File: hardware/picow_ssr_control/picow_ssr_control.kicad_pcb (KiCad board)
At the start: 2 copper layers, 65 x 90 mm, 25 parts, among them Q1 IRF4905, U1 RaspberryPi-PicoW, U2 ULN2803A

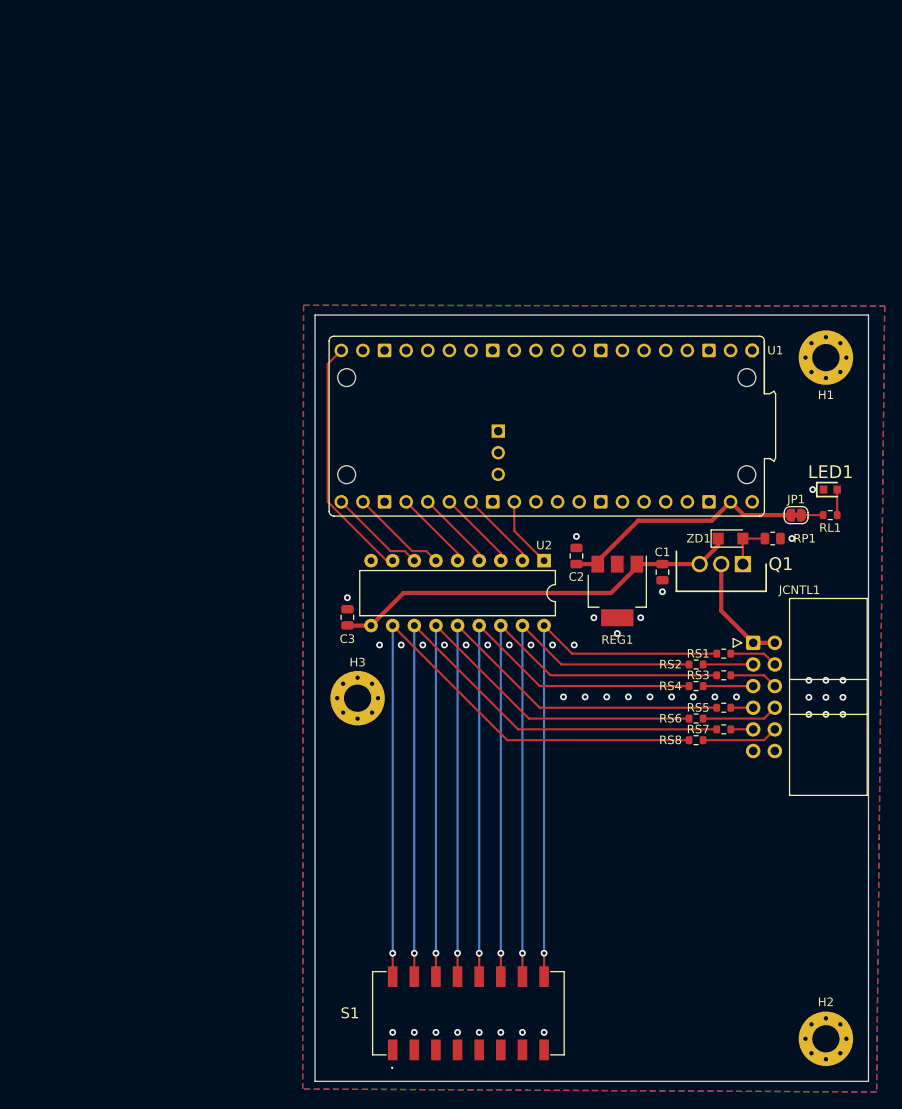
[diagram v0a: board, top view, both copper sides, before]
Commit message: Added Copyright and logos etc.
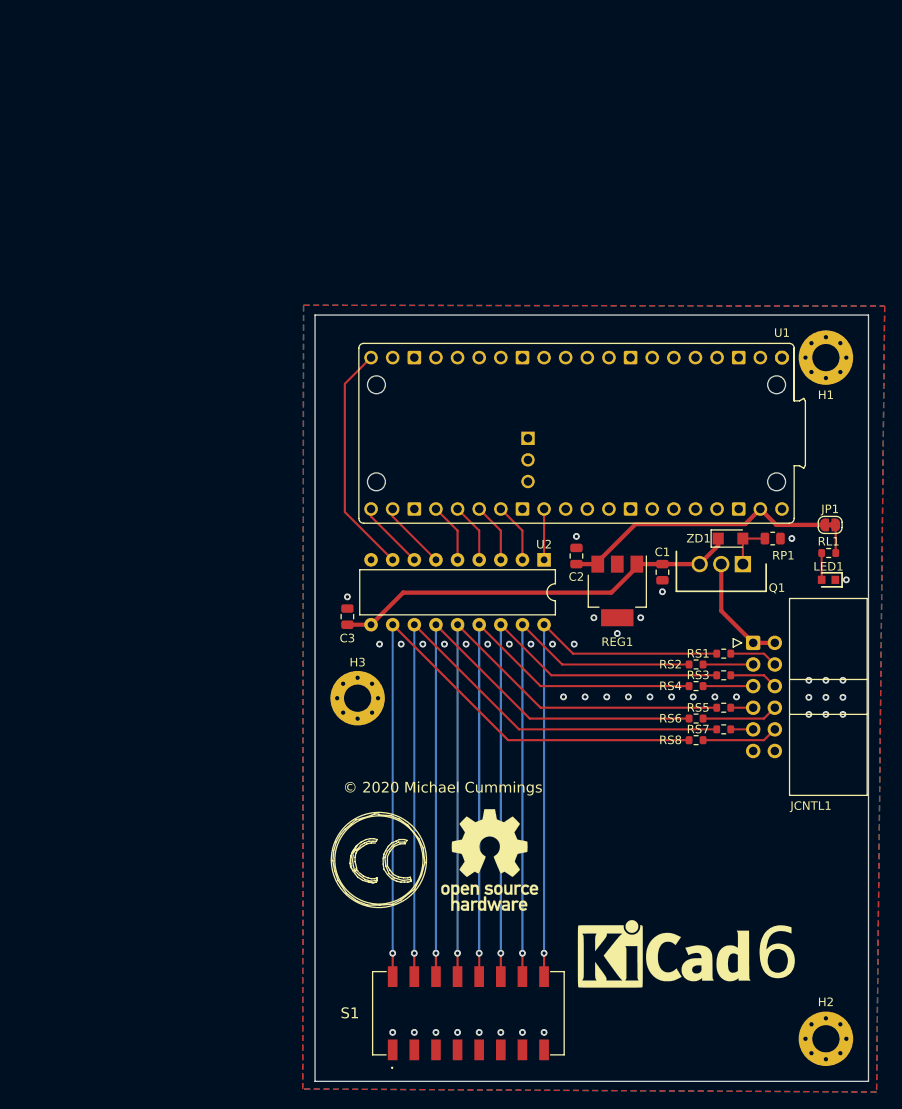
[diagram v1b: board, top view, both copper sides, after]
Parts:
- added #LOGO1: OSHW-Logo_11.4x12mm_SilkScreen, Symbol:OSHW-Logo_11.4x12mm_SilkScreen, F.Cu at (70.5, 114.0)
- added #LOGO2: KiCad-Logo_8mm_SilkScreen, Symbol:KiCad-Logo_8mm_SilkScreen, F.Cu at (91.0, 125.0)
- added #LOGO2: Symbol_CreativeCommons_SilkScreenTop_Type2_Big, Symbol:Symbol_CreativeCommons_SilkScreenTop_Type2_Big, F.Cu at (57.5, 114.0)
- moved LED1 10.6 mm to (110.3, 81.1), turned to 180 degrees
- moved RL1 4.45 mm to (110.3, 78.0), turned to 180 degrees
- moved JP1 4.16 mm to (110.5, 74.7)
- moved U1 3.59 mm to (104.8, 55.0)
- moved U2 0.10 mm to (76.9, 78.8)
- moved C3 0.08 mm to (53.8, 85.4)
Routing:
- net +5V: track 29.0 -> 32.5 mm
- net Net-(U1-Pad22): track 11.4 -> 8.07 mm
- net Net-(U1-Pad21): track 11.4 -> 8.07 mm
- net Net-(U1-Pad29): track 8.36 -> 5.97 mm
- net Net-(U1-Pad26): track 9.41 -> 7.02 mm
- net Net-(U1-Pad24): track 9.41 -> 7.02 mm
- net Net-(U1-Pad25): track 9.41 -> 7.02 mm
- net Net-(U1-Pad27): track 9.41 -> 7.02 mm
- net Net-(U1-Pad20): track 28.9 -> 27.4 mm
- net Net-(JP1-Pad2): track 2.52 -> 3.30 mm
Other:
- board text added: "0.2000 mm / 0.0000 mm"
- board text added: "0.3000 mm"
- board text added: "1.7600 mm"
- board text added: "2"
- board text added: "6"
- board text added: "65.0000 mm x 90.0000 mm"
- board text added: "BOARD CHARACTERISTICS"
- board text added: "Board Thickness:"
- board text added: "Board overall dimensions:"
- board text added: "Castellated pads:"
- board text added: "Copper Finish:"
- board text added: "Copper Layer Count:"
- board text added: "Edge card connectors:"
- board text added: "HAL lead-free"
- board text added: "Impedance Control:"
- board text added: "Min hole diameter:"
- board text added: "Min track/spacing:"
- board text added: "No"
- board text added: "Plated Board Edge:"
- board text added: "© 2020 Michael Cummings"

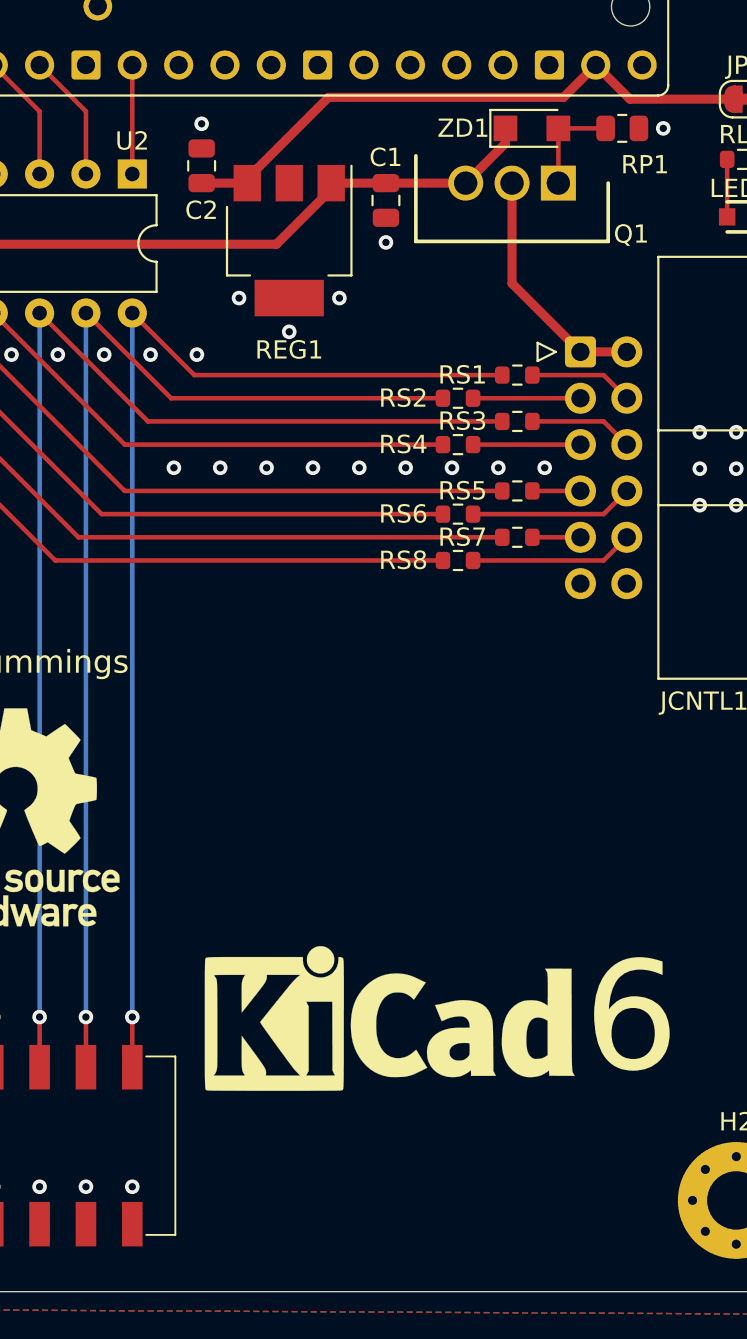
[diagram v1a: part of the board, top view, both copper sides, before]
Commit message: Added Updated symbol, footprint, 3d model for zener diode
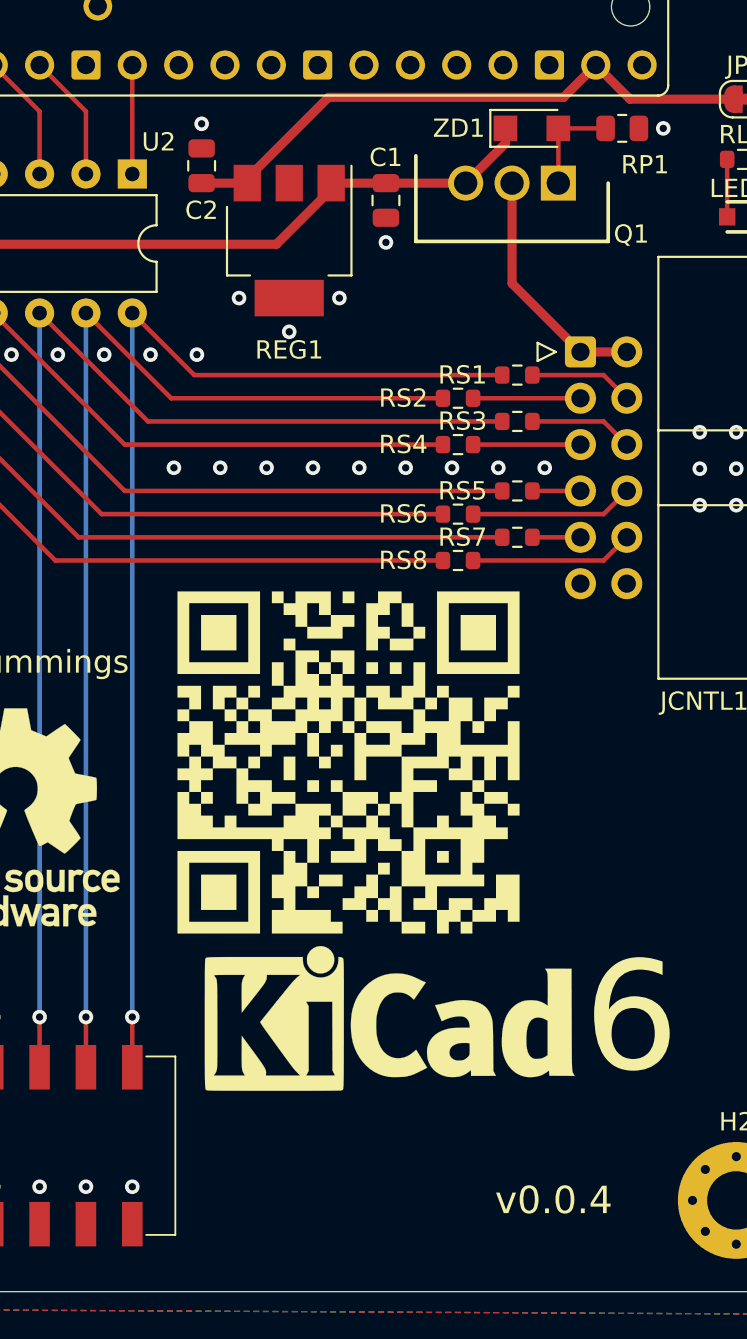
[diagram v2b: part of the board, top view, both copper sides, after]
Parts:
- added QRCode1: LOGO, LOGO, F.Cu at (88.8, 111.0)
- ZD1: footprint Diode_SMD:D_SMF -> Picow_control:BZD27C10P-M3-08
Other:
- board text added: "v0.0.4"

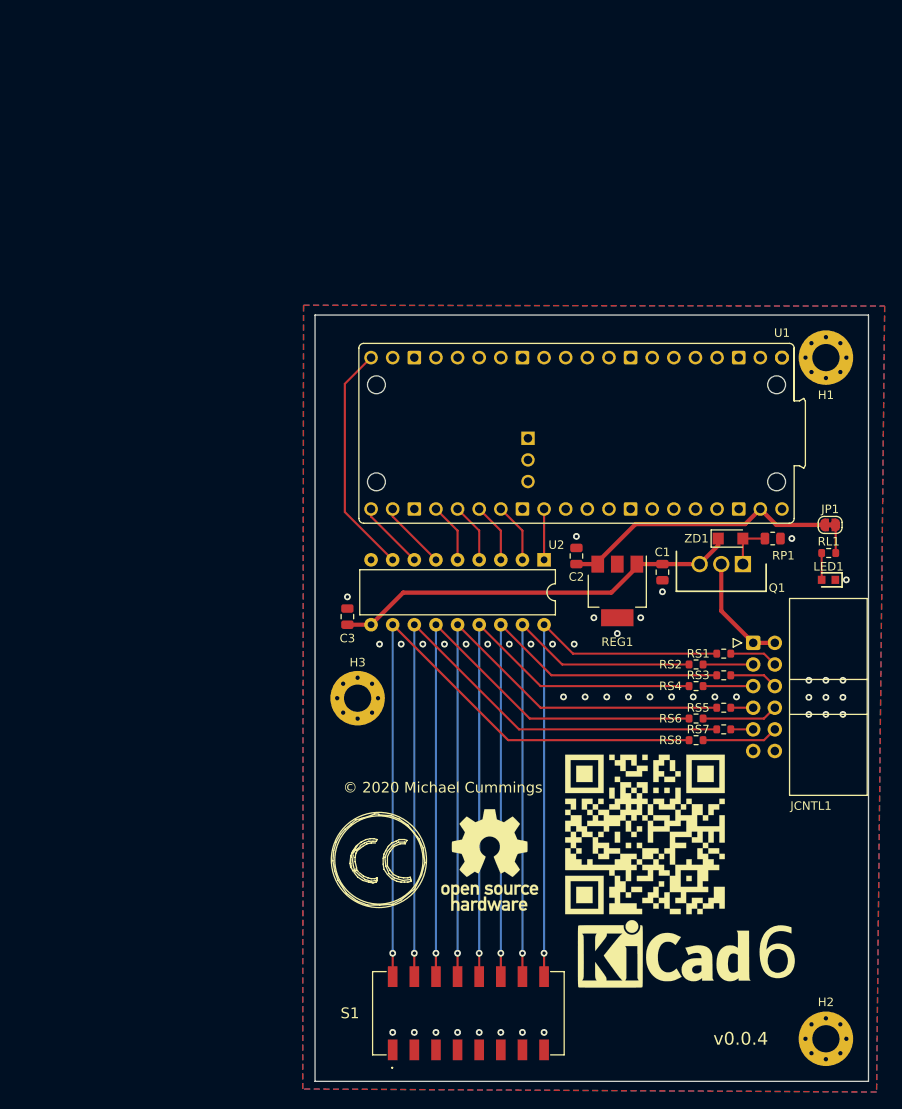
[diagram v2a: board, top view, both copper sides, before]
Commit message: Add new Cern licensing info
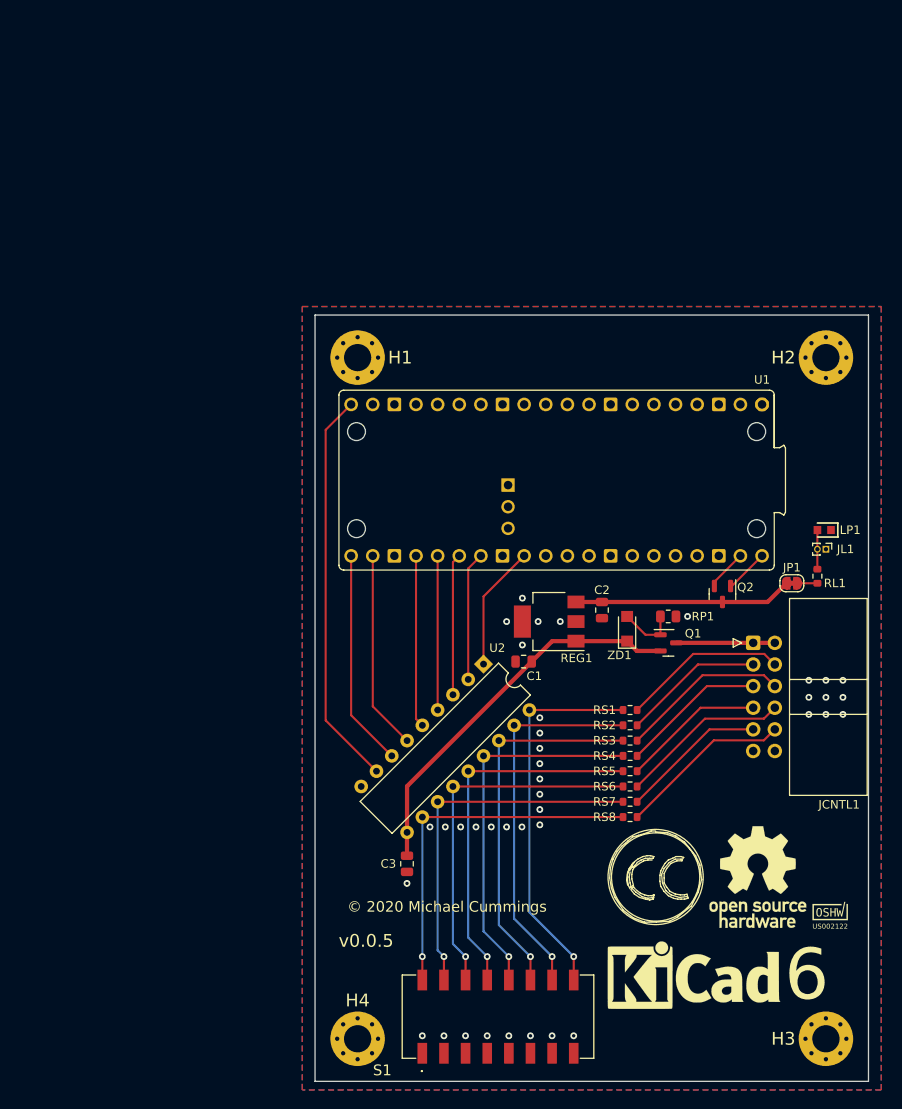
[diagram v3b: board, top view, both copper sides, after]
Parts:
- removed LED1: LTST-C190KGKT, dragon_mobile:LEDC1608X80N
- added H4: MountingHole_Pad, MountingHole:MountingHole_3.2mm_M3_Pad_Via, F.Cu at (55.0, 135.0)
- added JL1: Conn_01x02, Connector_PinHeader_1.00mm:PinHeader_1x02_P1.00mm_Vertical, F.Cu at (110.0, 77.5)
- added LP1: LTST-C190KGKT, dragon_mobile:LEDC1608X80N, F.Cu at (109.8, 75.2)
- added OSHW_Mono_0.1_Scale: US002122, Picow_control:OSHW_Mono_0.1_Scale, F.Cu at (110.5, 120.0)
- added Q2: DMG2301L, Package_TO_SOT_SMD:SOT-23, F.Cu at (97.8, 82.8)
- Q1: value IRF4905 -> DMG2301L; footprint dragon_mobile:TO254P469X1042X1967-3P -> Package_TO_SOT_SMD:SOT-23
- QRCode1: moved to B.Cu
- moved H2 80.0 mm to (110.0, 55.0)
- moved H3 68.0 mm to (110.0, 135.0)
- moved H1 55.0 mm to (55.0, 55.0)
- moved #LOGO2 32.6 mm to (90.0, 116.0)
- moved #LOGO1 31.6 mm to (102.0, 116.0)
- moved C3 29.9 mm to (60.8, 114.5), turned to -90 degrees
- moved C1 19.4 mm to (74.5, 90.7), turned to 180 degrees
- moved ZD1 16.1 mm to (86.7, 86.8), turned to 90 degrees
- moved RP1 15.3 mm to (91.5, 85.4)
- moved U2 14.2 mm to (69.8, 91.0), turned to -45 degrees
- moved RS7 13.9 mm to (87.0, 107.2)
- moved RS3 13.4 mm to (87.0, 100.0)
- moved RS5 13.3 mm to (87.0, 103.6)
- moved RS1 12.8 mm to (87.0, 96.4)
- moved Q1 12.7 mm to (91.5, 88.5), turned to 0 degrees
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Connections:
- Q1 pad 2: +BATT -> +VDC
- Q1 pad 3: +VDC -> +BATT
- U1 pad 39: +5V -> Net-(Q2-Pad2)
- U1 pad 40: unconnected-(U1-Pad40) -> Net-(Q2-Pad1)
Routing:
- net /a8: track 81.8 -> 42.7 mm
- net /a7: track 81.9 -> 43.0 mm
- net /a6: track 75.6 -> 43.3 mm
- net /a5: track 75.8 -> 43.6 mm
- net /a4: track 69.0 -> 43.9 mm
- net /a3: track 69.1 -> 44.2 mm
- net Net-(U1-Pad20): track 27.4 -> 46.8 mm
- net /a2: track 62.8 -> 44.6 mm
- net /a1: track 63.0 -> 44.9 mm
- net Net-(U1-Pad21): track 8.07 -> 25.5 mm
- net Net-(U1-Pad22): track 8.07 -> 23.4 mm
- net Net-(JCNTL1-Pad9): track 2.63 -> 17.2 mm
- net Net-(JCNTL1-Pad6): track 5.70 -> 19.9 mm
- net Net-(JCNTL1-Pad7): track 2.63 -> 16.7 mm
- net Net-(JCNTL1-Pad4): track 5.70 -> 19.4 mm
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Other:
- board text added: "+"
- board text added: "Mounting holes are for M3 screws and should be drill at 2.5mm (#39) and tapped at .5mm threads."
- board text added: "v0.0.5"
- board text removed: "v0.0.4"

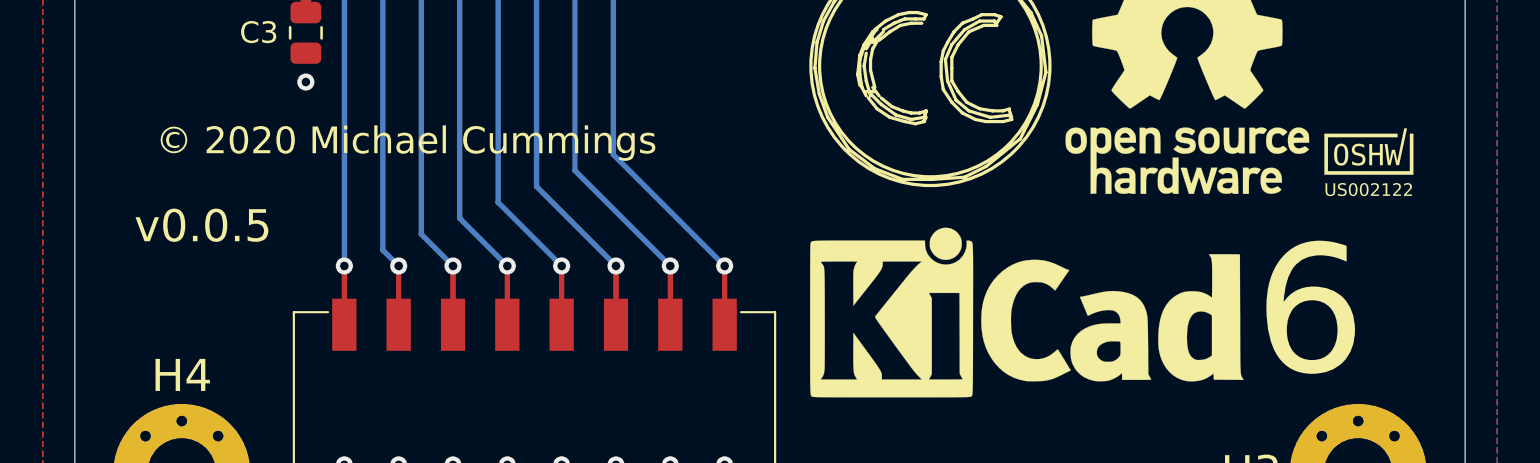
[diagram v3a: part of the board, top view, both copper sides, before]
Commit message: Synced up schema and PCB versions and Licensing silkscreening
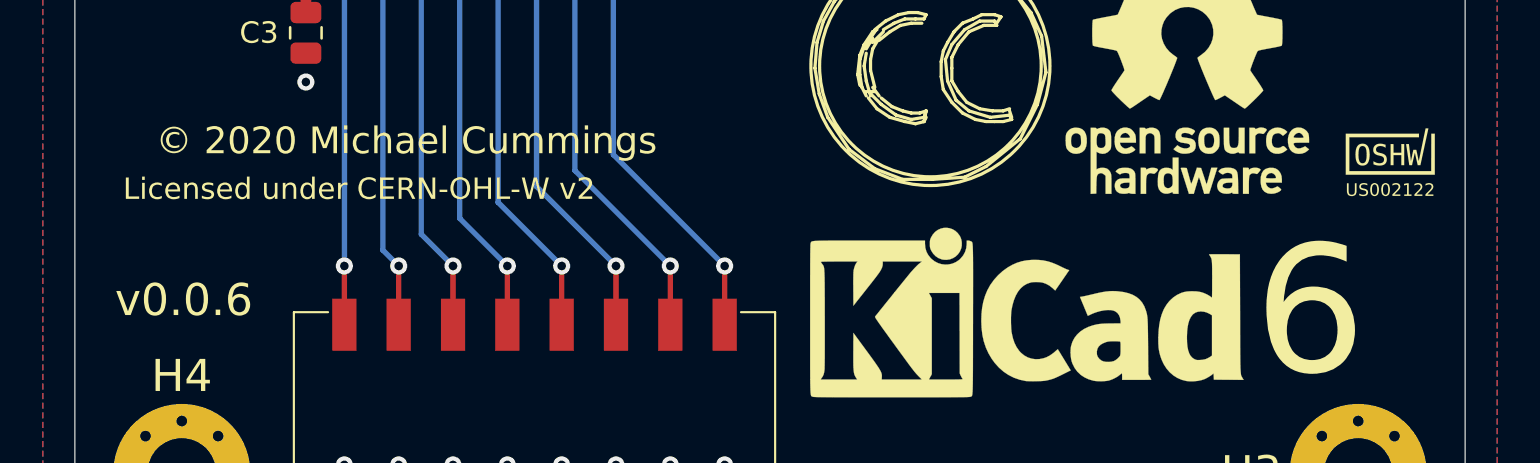
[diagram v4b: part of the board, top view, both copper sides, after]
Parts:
- moved OSHW_Mono_0.1_Scale 1.00 mm to (111.5, 120.0)
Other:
- board text added: "Licensed under CERN-OHL-W v2"
- board text added: "v0.0.6"
- board text removed: "v0.0.5"
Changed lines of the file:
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@@
   (title_block
     (title "Picow SSR Control")
-    (date "2022-08-01")
-    (rev "0.0.5")
+    (date "2022-08-05")
+    (rev "0.0.6")
     (comment 2 "http://creativecommons.org/licenses/by-sa/4.0/")
     (comment 3 "License: CC By SA 4.0")
     (comment 4 "Author: Michael Cummings")
+    (comment 5 "https://ohwr.org/project/cernohl/wikis/Documents/CERN-OHL-version-2")
+    (comment 6 "Hardware License: CERN-OHL-W")
   )
   (layers
@@
   )
   (footprint "Picow_control:OSHW_Mono_0.1_Scale" (layer "F.Cu")
-    (at 110.5 120)
+    (at 111.5 120)
     (attr board_only exclude_from_pos_files exclude_from_bom)
     (fp_text reference "OSHW_Mono_0.1_Scale" (at 0 -4.132151) (layer "F.SilkS") hide
@@
     (effects (font (size 1.25 1.25) (thickness 0.25)))
   )
-  (gr_text "v0.0.5" (at 56 123.5) (layer "F.SilkS")
+  (gr_text "Licensed under CERN-OHL-W v2" (at 52.25 121.75) (layer "F.SilkS")
+    (effects (font (size 1 1) (thickness 0.15)) (justify left))
+  )
+  (gr_text "v0.0.6" (at 55.1 126.95) (layer "F.SilkS")
     (effects (font (size 1.5 1.5) (thickness 0.25)))
   )
